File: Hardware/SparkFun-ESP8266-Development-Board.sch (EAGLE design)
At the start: 70 parts, among them J1 U.FL, Q1 2.5A/30V, Q2 MMBT2222A, U1 ESP8266, U2 MCP73831, U3 AT25SF041-SOIC8, U4 AP2112K-3.3V, U5 ATECC108-SSHDA, Y1 26MHz

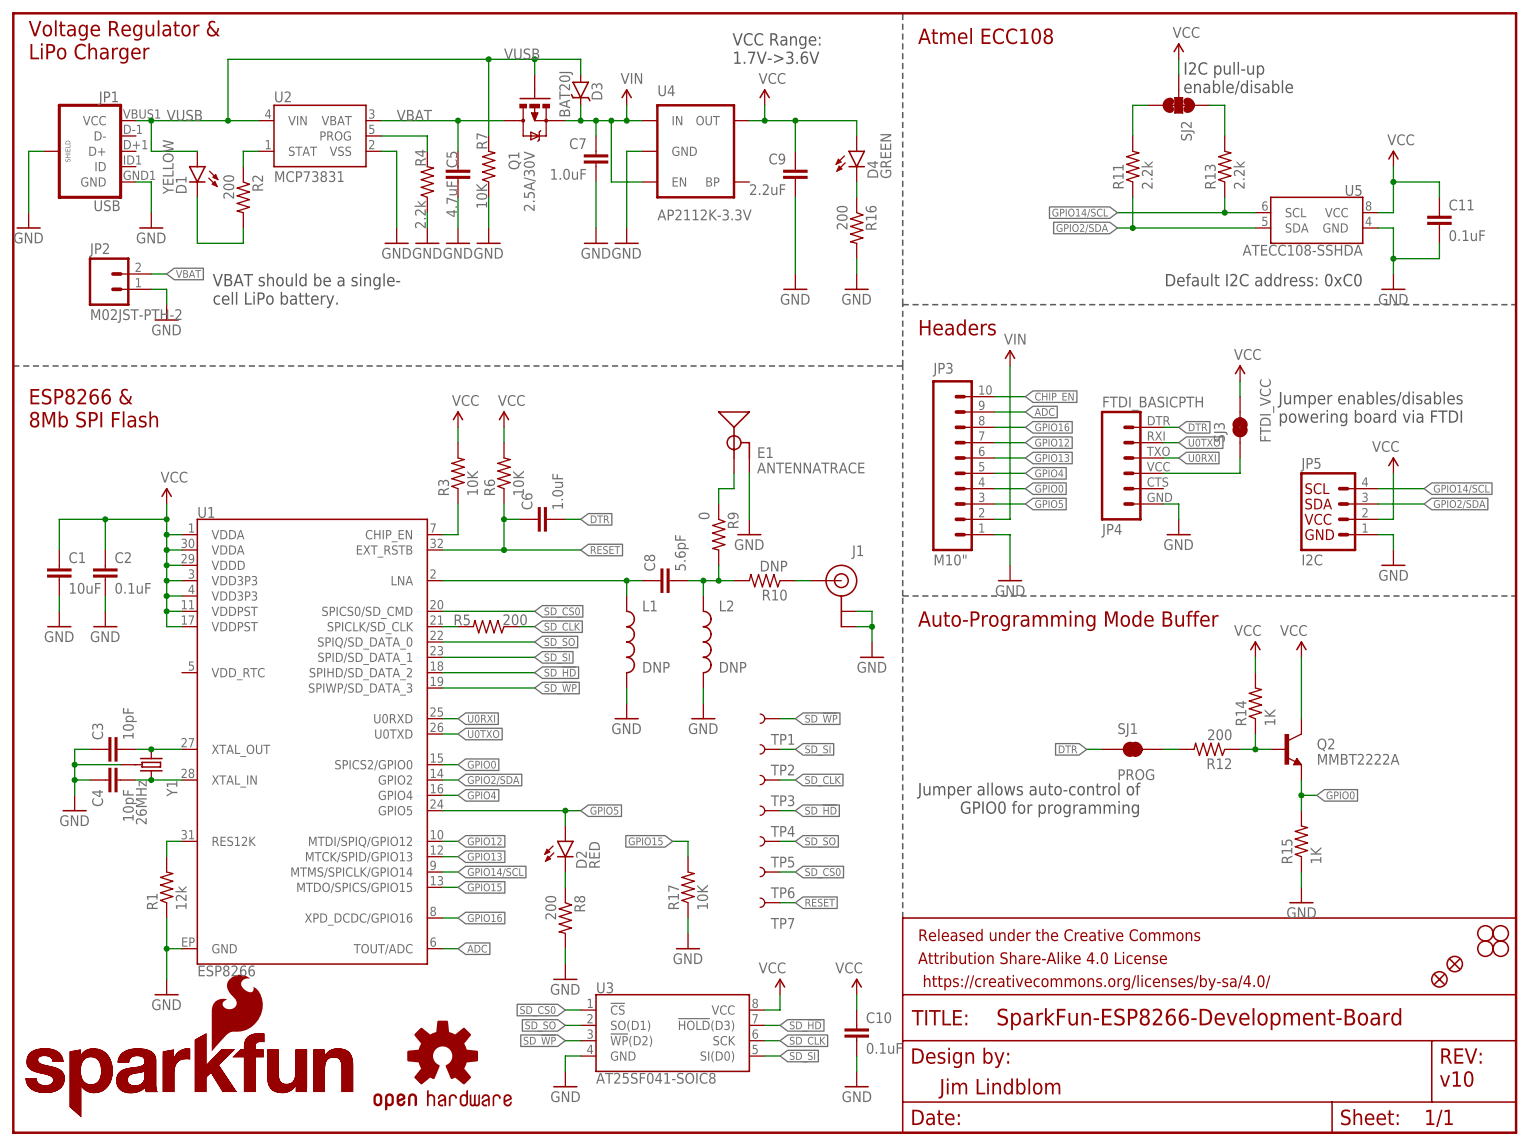
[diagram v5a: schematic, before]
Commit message: Adding light and temperature sensors. Adding ON/OFF switch. Simplifying DTR-GPIO0 circuit.
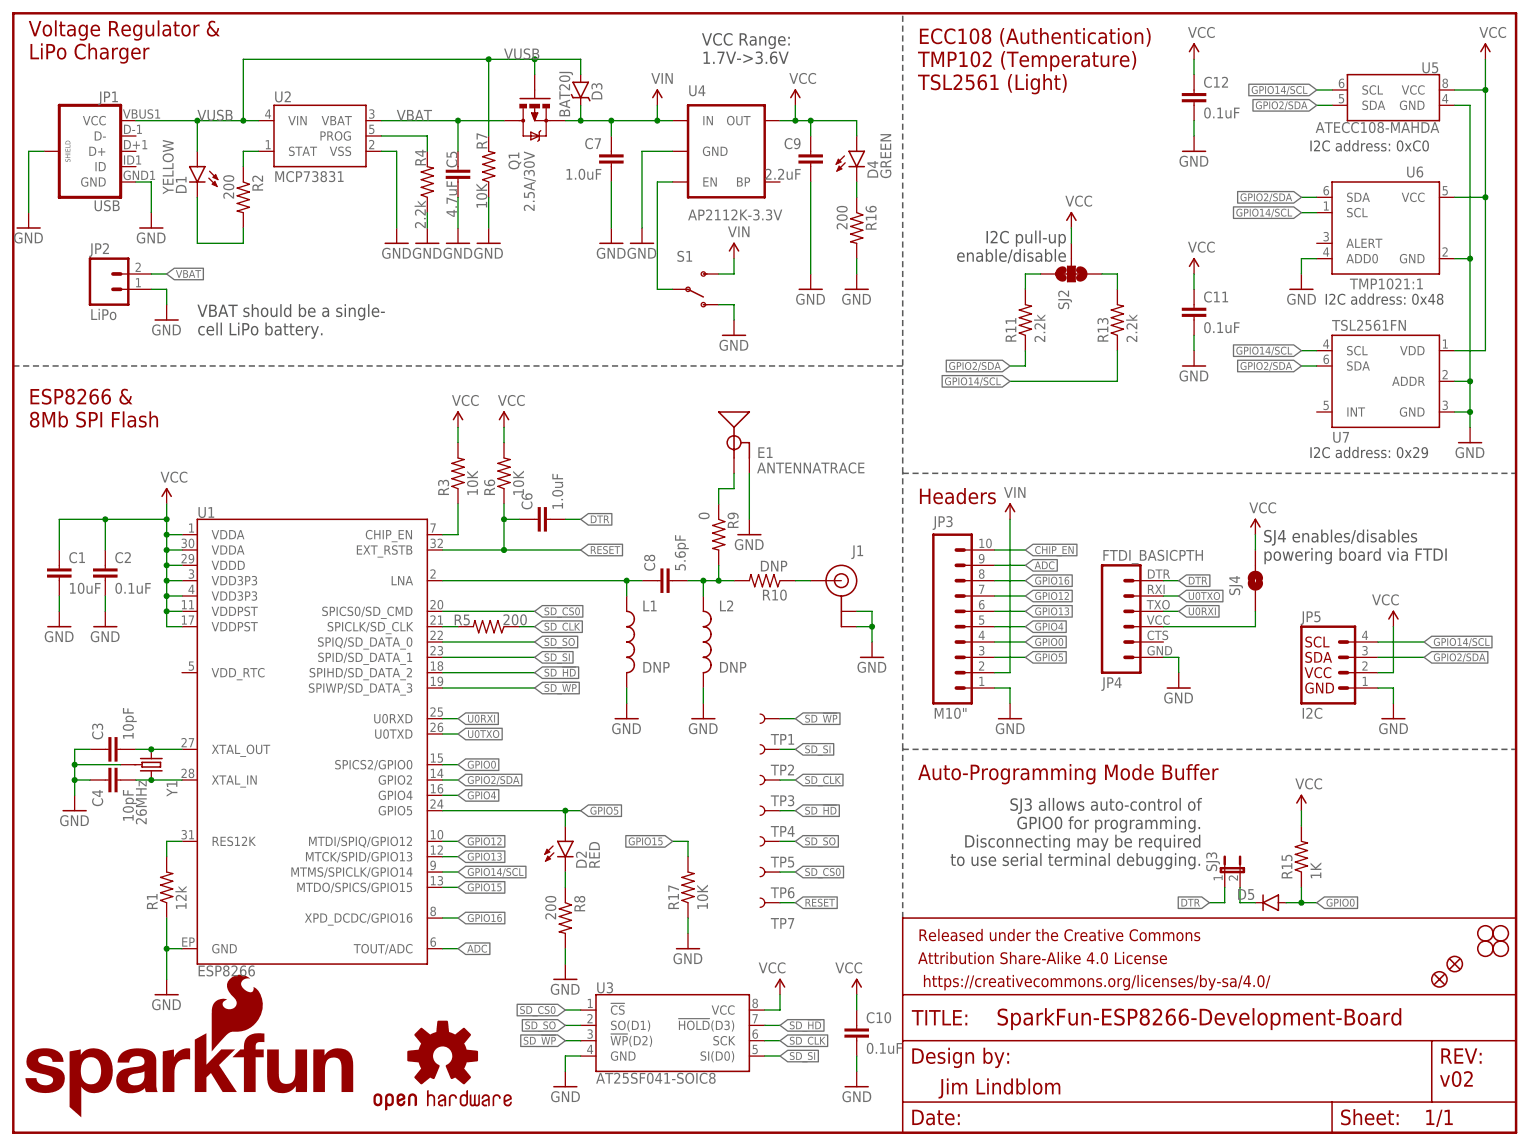
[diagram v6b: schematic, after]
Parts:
- removed LOGO2: SFE_LOGO_NAME.1_INCH, SparkFun-Aesthetics:SFE_LOGO_NAME.1_INCH
- removed Q2: MMBT2222A, SparkFun-DiscreteSemi:TRANSISTOR_NPNMMBT2222A
- removed R12: 200, SparkFun-Resistors:200OHM1/10W1%(0603)
- removed R14: 1K, SparkFun-Resistors:1KOHM1/10W1%(0603)
- removed SJ1: PROG, SparkFun-Passives:JUMPER-PAD-2-NC_BY_TRACE
- added C12: 0.1uF, SparkFun-Capacitors:0.1UF-25V(+80/-20%)(0603)
- added D5: (no value), SparkFun-DiscreteSemi:DIODEBAS16
- added S1: (no value), SparkFun-Electromechanical:SWITCH-SPDT-SMD-A
- added SJ4: JUMPER-PAD-2-NOYES_SILK, SparkFun-Passives:JUMPER-PAD-2-NOYES_SILK
- added U6: TMP1021:1, SparkFun-Sensors:TMP1021:1
- added U7: TSL2561FN, esp8266-development-board:TSL2561FN
- JP2: value M02JST-PTH-2 -> LiPo
- LOGO1: value SFE_LOGO_NAME.1_INCH -> SFE_LOGO_NAME.2_INCH; device SparkFun-Aesthetics:SFE_LOGO_NAME.1_INCH -> SparkFun-Aesthetics:SFE_LOGO_NAME.2_INCH
- SJ3: value FTDI_VCC -> JUMPER-PTH-2-NC; device SparkFun-Passives:JUMPER-PAD-2-NC_BY_TRACE -> SparkFun-Passives:JUMPER-PTH-2-NC
- U5: value ATECC108-SSHDA -> ATECC108-MAHDA; device esp8266-development-board:ATECC108-SSHDA -> esp8266-development-board:ATECC108-MAHDA
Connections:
- removed net N$8: R12.2, SJ1.2
- new net N$11: S1.P, U4.EN
- net DTR: now also SJ3.1; no longer SJ1.1
- net FTDI_VCC: now also SJ4.1; no longer SJ3.1
- net GND: now also C12.2, S1.O, U6.ADD0, U6.GND, U7.ADDR, U7.GND; no longer R15.1
- net GPIO0: now also D5.A, R15.1; no longer Q2.E, R15.2
- net GPIO14/SCL: now also U6.SCL, U7.SCL
- net GPIO2/SDA: now also U6.SDA, U7.SDA
- net N$10: now also SJ2.3; no longer SJ2.1
- net N$7: now also D5.C, SJ3.2; no longer Q2.B, R12.1, R14.1
- net N$9: now also SJ2.1; no longer SJ2.3
- net VCC: now also C12.1, R15.2, SJ4.2, U6.VCC, U7.VDD; no longer Q2.C, R14.2, SJ3.2
- net VIN: now also S1.S; no longer U4.EN
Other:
- note added: "ECC108 (Authentication) TMP102 (Temperature) TSL2561 (Light)"
- note added: "I2C address: 0x29"
- note added: "I2C address: 0x48"
- note added: "I2C address: 0xC0"
- note added: "SJ3 allows auto-control of GPIO0 for programming. Disconnecting may be required to use serial terminal debugging."
- note added: "SJ4 enables/disables powering board via FTDI"
- note added: "v02"
- note removed: "Atmel ECC108"
- note removed: "Default I2C address: 0xC0"
- note removed: "Jumper allows auto-control of GPIO0 for programming"
- note removed: "Jumper enables/disables powering board via FTDI"
- note removed: "v10"
- moved on the sheet: C11, C7, C9, JP3, JP4, JP5, R11, R13, R15, SJ2, U4, U5

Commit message: Swapping colors of PWR and pin 5 LEDs. Adding SMD jumper to GPIO0/DTR.
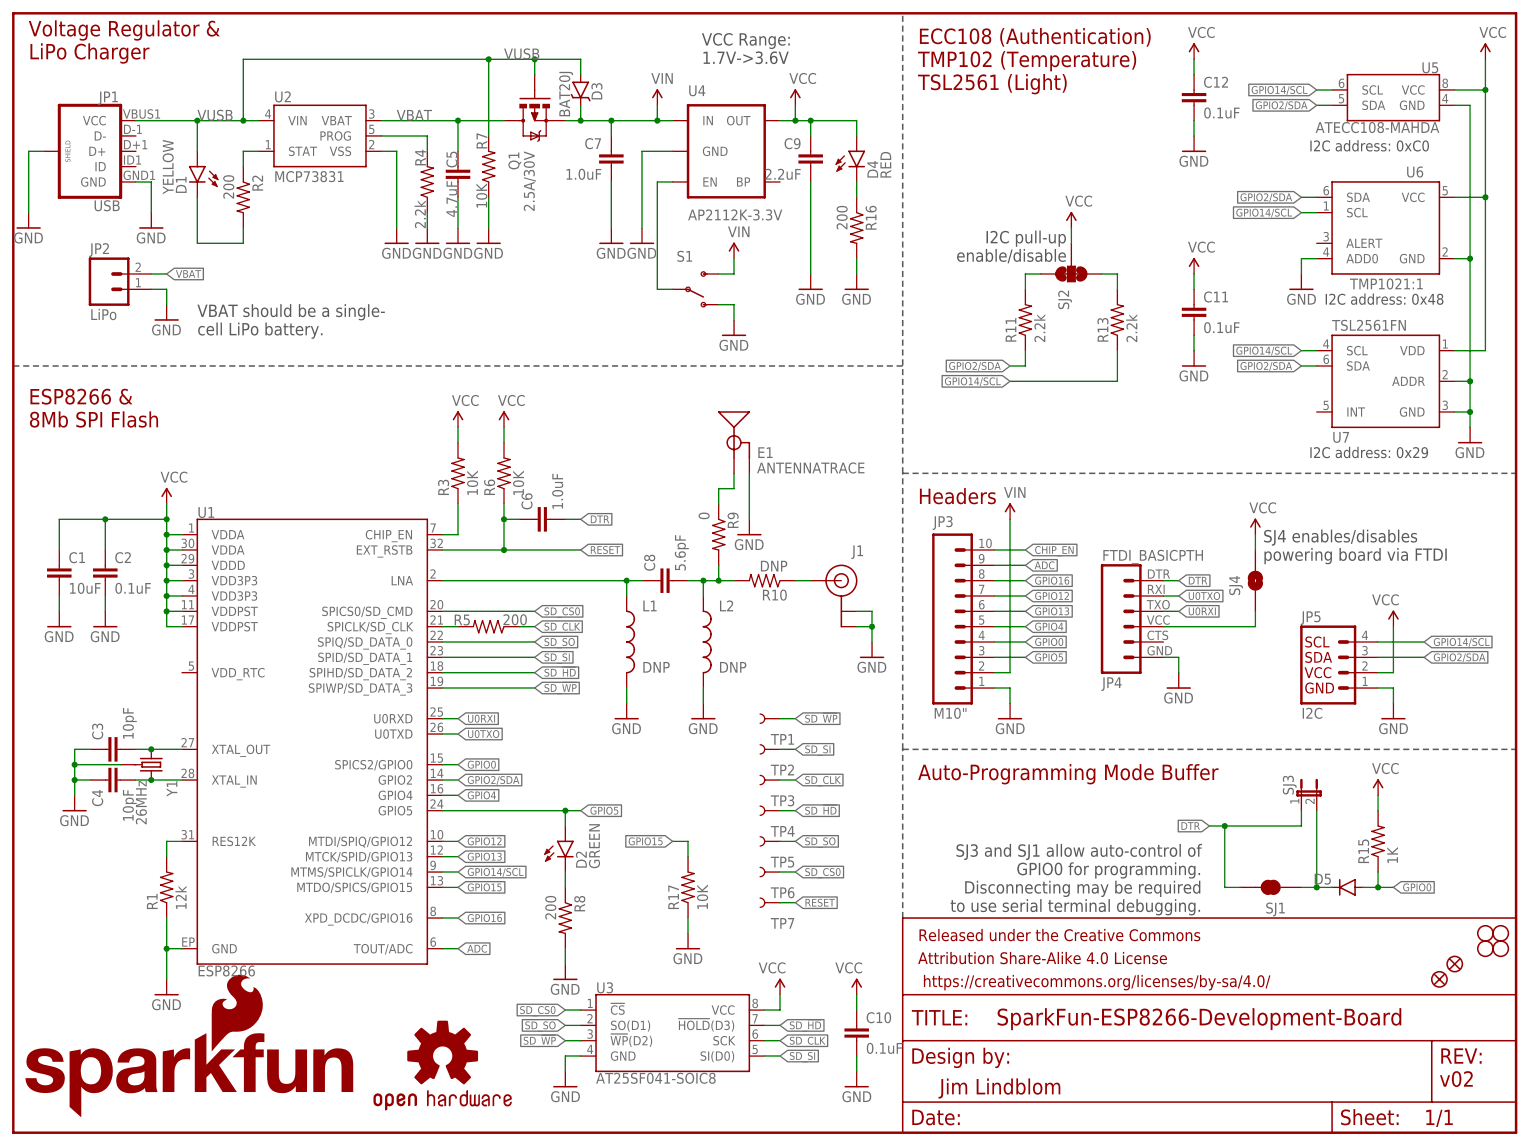
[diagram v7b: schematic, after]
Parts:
- added SJ1: JUMPER-PAD-2-NC_BY_TRACE, SparkFun-Passives:JUMPER-PAD-2-NC_BY_TRACE
- D2: value RED -> GREEN; device SparkFun-LED:LED-RED0603 -> SparkFun-LED:LED-GREEN0603
- D4: value GREEN -> RED; device SparkFun-LED:LED-GREEN0603 -> SparkFun-LED:LED-RED0603
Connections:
- net DTR: now also SJ1.2
- net N$7: now also SJ1.1
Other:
- note added: "SJ3 and SJ1 allow auto-control of GPIO0 for programming. Disconnecting may be required to use serial terminal debugging."
- note removed: "SJ3 allows auto-control of GPIO0 for programming. Disconnecting may be required to use serial terminal debugging."
- moved on the sheet: D5, R15, SJ3

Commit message: Revising silkscreen. Optimizing some traces. Updated to v10.
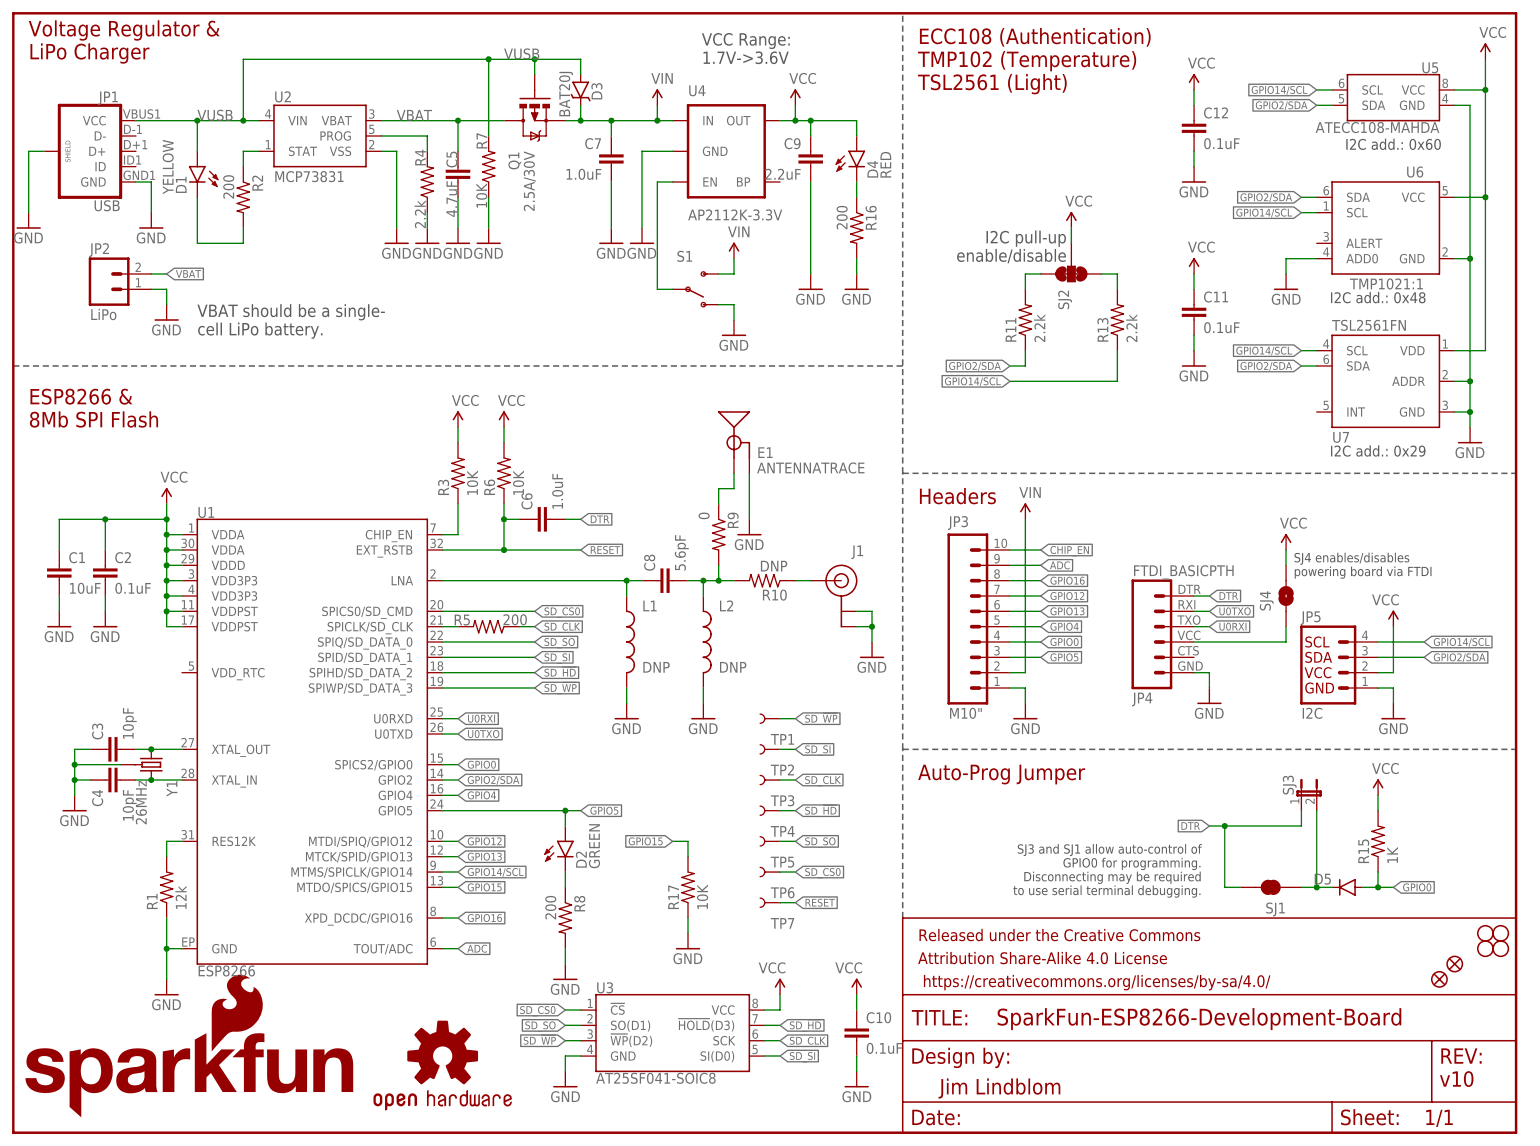
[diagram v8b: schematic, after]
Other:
- note added: "Auto-Prog Jumper"
- note added: "I2C add.: 0x29"
- note added: "I2C add.: 0x48"
- note added: "I2C add.: 0x60"
- note added: "v10"
- note removed: "Auto-Programming Mode Buffer"
- note removed: "I2C address: 0x29"
- note removed: "I2C address: 0x48"
- note removed: "I2C address: 0xC0"
- note removed: "v02"
- moved on the sheet: C12, JP3, JP4, SJ4
